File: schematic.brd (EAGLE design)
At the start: 160 x 58 mm, 39 parts, among them IC1 74HC595N, T8 BC337

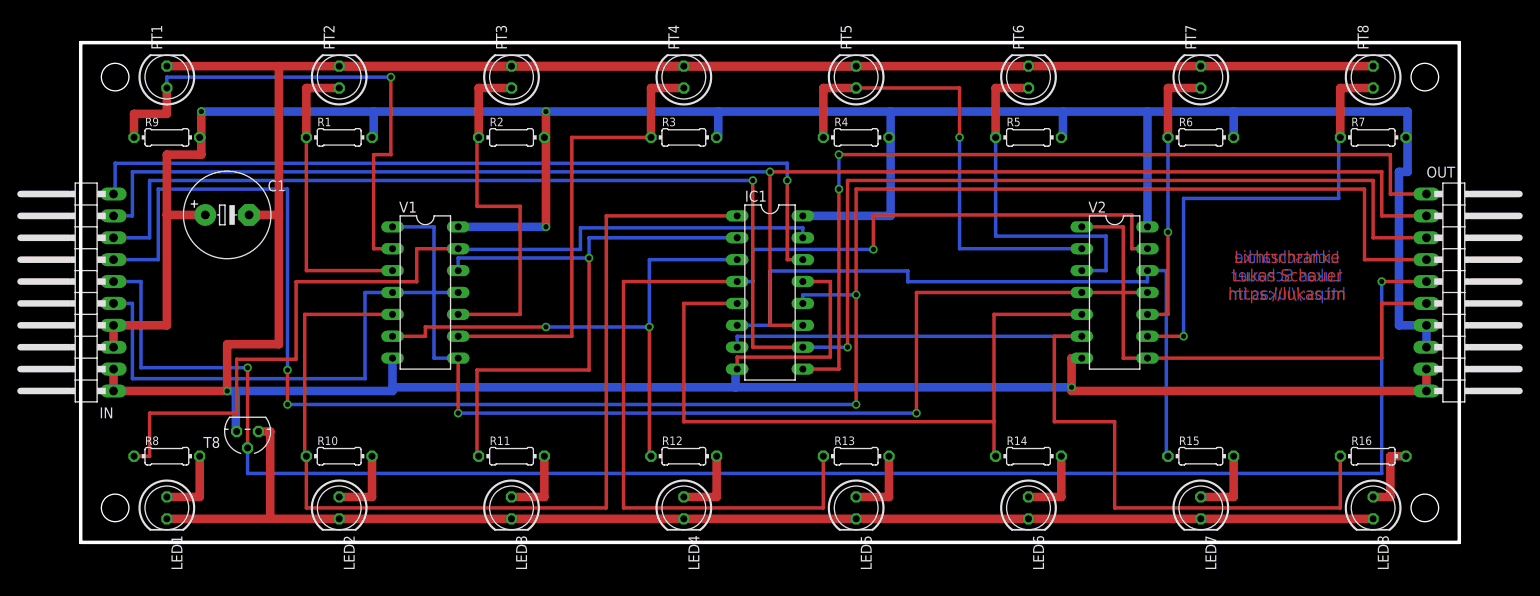
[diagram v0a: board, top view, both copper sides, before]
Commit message: fixed connection to ground plane, added ground stitching, added ground plane isolation
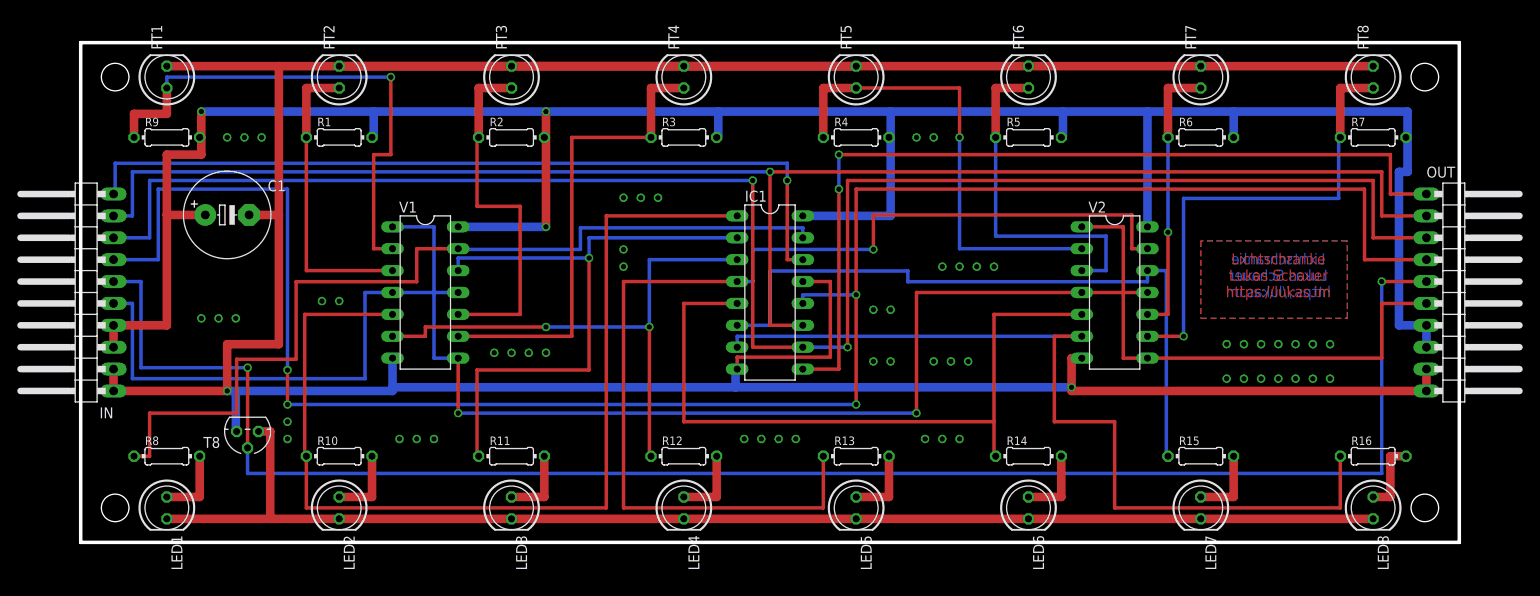
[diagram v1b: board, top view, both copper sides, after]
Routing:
- net GND: vias 2 -> 58
- added copper zone on layer 1, net GND
- added copper zone on layer 16, net GND
- added copper zone on layer 1, net N$7
- added copper zone on layer 16, net N$9
- removed copper zone on layer 16, net N$7
- removed copper zone on layer 1, net N$9
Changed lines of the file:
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@@
 <?xml version="1.0" encoding="utf-8"?>
 <!DOCTYPE eagle SYSTEM "eagle.dtd">
-<eagle version="7.6.0">
+<eagle version="7.7.0">
 <drawing>
 <settings>
@@
 <hole x="156" y="54" drill="3.2"/>
 <hole x="156" y="4" drill="3.2"/>
-<text x="140" y="31" size="1.4224" layer="1" font="vector" align="center">Lichtschranke
+<text x="139" y="31" size="1.27" layer="1" font="vector" align="center">Lichtschranke
 Lukas Schauer
 https://lukas.im</text>
-<text x="140" y="31" size="1.4224" layer="16" font="vector" rot="MR0" align="center">Lichtschranke
+<text x="139" y="31" size="1.27" layer="16" font="vector" rot="MR0" align="center">Lichtschranke
 Lukas Schauer
 https://lukas.im</text>
@@
 <contactref element="C1" pad="-"/>
 <wire x1="19.54" y1="38" x2="23" y2="38" width="1" layer="1"/>
+<polygon width="0.4064" layer="16" isolate="0.4064">
+<vertex x="0" y="58"/>
+<vertex x="160" y="58"/>
+<vertex x="160" y="0"/>
+<vertex x="0" y="0"/>
+</polygon>
+<polygon width="0.4064" layer="1" isolate="0.4064">
+<vertex x="0" y="58"/>
+<vertex x="160" y="58"/>
+<vertex x="160" y="0"/>
+<vertex x="0" y="0"/>
+</polygon>
+<via x="133" y="23" extent="1-16" drill="0.6"/>
+<via x="135" y="23" extent="1-16" drill="0.6"/>
+<via x="137" y="23" extent="1-16" drill="0.6"/>
+<via x="139" y="23" extent="1-16" drill="0.6"/>
+<via x="141" y="23" extent="1-16" drill="0.6"/>
+<via x="143" y="23" extent="1-16" drill="0.6"/>
+<via x="145" y="23" extent="1-16" drill="0.6"/>
+<via x="145" y="19" extent="1-16" drill="0.6"/>
+<via x="143" y="19" extent="1-16" drill="0.6"/>
+<via x="141" y="19" extent="1-16" drill="0.6"/>
+<via x="139" y="19" extent="1-16" drill="0.6"/>
+<via x="135" y="19" extent="1-16" drill="0.6"/>
+<via x="137" y="19" extent="1-16" drill="0.6"/>
+<via x="133" y="19" extent="1-16" drill="0.6"/>
+<via x="77" y="12" extent="1-16" drill="0.6"/>
+<via x="79" y="12" extent="1-16" drill="0.6"/>
+<via x="81" y="12" extent="1-16" drill="0.6"/>
+<via x="83" y="12" extent="1-16" drill="0.6"/>
+<via x="98" y="12" extent="1-16" drill="0.6"/>
+<via x="100" y="12" extent="1-16" drill="0.6"/>
+<via x="102" y="12" extent="1-16" drill="0.6"/>
+<via x="99" y="21" extent="1-16" drill="0.6"/>
+<via x="101" y="21" extent="1-16" drill="0.6"/>
+<via x="103" y="21" extent="1-16" drill="0.6"/>
+<via x="106" y="32" extent="1-16" drill="0.6"/>
+<via x="104" y="32" extent="1-16" drill="0.6"/>
+<via x="102" y="32" extent="1-16" drill="0.6"/>
+<via x="100" y="32" extent="1-16" drill="0.6"/>
+<via x="94" y="27" extent="1-16" drill="0.6"/>
+<via x="92" y="27" extent="1-16" drill="0.6"/>
+<via x="94" y="21" extent="1-16" drill="0.6"/>
+<via x="92" y="21" extent="1-16" drill="0.6"/>
+<via x="24" y="14" extent="1-16" drill="0.6"/>
+<via x="24" y="12" extent="1-16" drill="0.6"/>
+<via x="48" y="22" extent="1-16" drill="0.6"/>
+<via x="50" y="22" extent="1-16" drill="0.6"/>
+<via x="52" y="22" extent="1-16" drill="0.6"/>
+<via x="54" y="22" extent="1-16" drill="0.6"/>
+<via x="30" y="28" extent="1-16" drill="0.6"/>
+<via x="28" y="28" extent="1-16" drill="0.6"/>
+<via x="97" y="47" extent="1-16" drill="0.6"/>
+<via x="99" y="47" extent="1-16" drill="0.6"/>
+<via x="17" y="47" extent="1-16" drill="0.6"/>
+<via x="19" y="47" extent="1-16" drill="0.6"/>
+<via x="21" y="47" extent="1-16" drill="0.6"/>
+<via x="14" y="26" extent="1-16" drill="0.6"/>
+<via x="16" y="26" extent="1-16" drill="0.6"/>
+<via x="18" y="26" extent="1-16" drill="0.6"/>
+<via x="37" y="12" extent="1-16" drill="0.6"/>
+<via x="39" y="12" extent="1-16" drill="0.6"/>
+<via x="41" y="12" extent="1-16" drill="0.6"/>
+<via x="63" y="40" extent="1-16" drill="0.6"/>
+<via x="65" y="40" extent="1-16" drill="0.6"/>
+<via x="67" y="40" extent="1-16" drill="0.6"/>
+<via x="63" y="34" extent="1-16" drill="0.6"/>
+<via x="63" y="32" extent="1-16" drill="0.6"/>
+<wire x1="63" y1="34" x2="63" y2="32" width="0" layer="19" extent="1-1"/>
 </signal>
 <signal name="N$10">
@@
 </signal>
 <signal name="N$7">
-<polygon width="0.4064" layer="16">
-<vertex x="0" y="58"/>
-<vertex x="160" y="58"/>
-<vertex x="160" y="0"/>
-<vertex x="0" y="0"/>
+<polygon width="0.8128" layer="1" pour="cutout" isolate="0.6096">
+<vertex x="130" y="35"/>
+<vertex x="130" y="26"/>
+<vertex x="147" y="26"/>
+<vertex x="147" y="35"/>
 </polygon>
 </signal>
 <signal name="N$9">
-<polygon width="0.4064" layer="1">
-<vertex x="0" y="58"/>
-<vertex x="160" y="58"/>
-<vertex x="160" y="0"/>
-<vertex x="0" y="0"/>
+<polygon width="0.8128" layer="16" pour="cutout" isolate="0.6096">
+<vertex x="130" y="35"/>
+<vertex x="130" y="26"/>
+<vertex x="147" y="26"/>
+<vertex x="147" y="35"/>
 </polygon>
 </signal>
